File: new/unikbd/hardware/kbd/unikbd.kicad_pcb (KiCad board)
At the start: 2 copper layers, 304.8 x 152.4 mm, 140 parts, among them J1 Conn_01x16, SW1 Ampersand, SW10 Semicolon, SW11 M, SW12 J, SW14 Fwd_Slash, SW15 N, SW16 H, SW18 SPACE, SW19 B, SW20 G, SW21 ESC, SW22 Z, SW23 V, SW24 F, SW25 CTRL, SW26 A, SW27 C, SW28 D, SW29 Backslash, SW3 Break, SW30 Q, SW31 X, SW32 S, SW33 Clear, SW34 Repeat, SW35 Tilde, SW37 I, SW38 Here_is, SW39 Bracket_Close, SW4 Rubout, SW40 7, SW41 U, SW42 Shift_Lock, SW43 Bracket_Open, SW44 6, SW45 Y, SW46 Return, SW47 Dash, SW48 5, SW49 T, SW5 R_Shift, SW50 Line Feed, SW51 Colon, SW52 4, SW53 R, SW54 O, SW55 0, SW56 3, SW57 E, SW58 L, SW59 9, SW6 P, SW60 2, SW61 W, SW62 Period, SW63 8, SW64 1, SW7 Comma, SW8 K, SW9 L_Shift, U1 7402, U2 74LS240, U3 74LS240, U4 74LS373

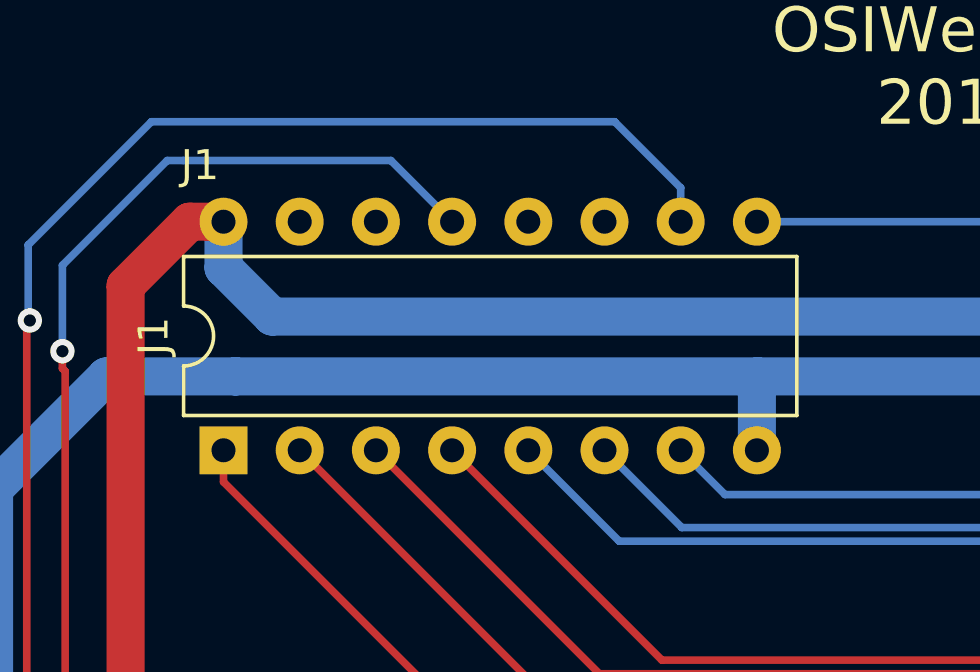
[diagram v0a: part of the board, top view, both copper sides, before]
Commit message: updated connector J1 footprint to socket
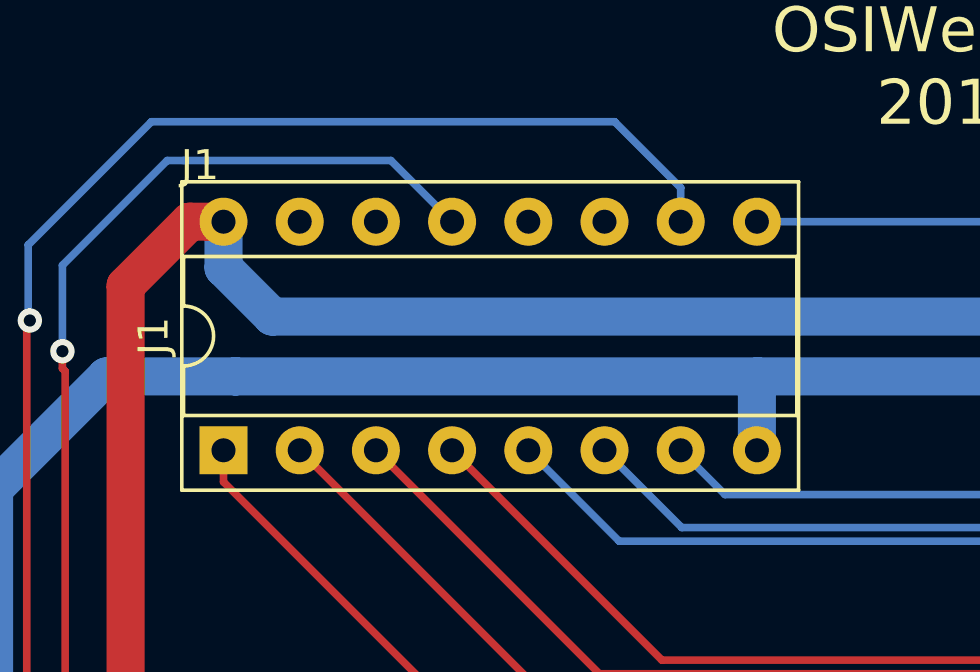
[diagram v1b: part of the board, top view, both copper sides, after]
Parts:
- J1: footprint Package_DIP:DIP-16_W7.62mm -> Package_DIP:DIP-16_W7.62mm_Socket
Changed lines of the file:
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@@
     (add_net /Col0)
+  )
+  (module Package_DIP:DIP-16_W7.62mm_Socket (layer F.Cu)
+    (at 77.9907 44.9072 90)
+    (descr "16-lead though-hole mounted DIP package, row spacing 7.62 mm (300 mils), Socket")
+    (tags "THT DIP DIL PDIP 2.54mm 7.62mm 300mil Socket")
+    (fp_text reference J1 (at 3.81 -2.33 90) (layer F.SilkS)
+      (effects (font (size 1 1) (thickness 0.15)))
+    )
+    (fp_text value Conn_01x16 (at 3.81 20.11 90) (layer F.Fab)
+      (effects (font (size 1 1) (thickness 0.15)))
+    )
+    (fp_text user %R (at 9.50214 -0.78486 180) (layer F.SilkS)
+      (effects (font (size 1 1) (thickness 0.15)))
+    )
+    (fp_line (start 9.15 -1.6) (end -1.55 -1.6) (layer F.CrtYd) (width 0.05))
+    (fp_line (start 9.15 19.4) (end 9.15 -1.6) (layer F.CrtYd) (width 0.05))
+    (fp_line (start -1.55 19.4) (end 9.15 19.4) (layer F.CrtYd) (width 0.05))
+    (fp_line (start -1.55 -1.6) (end -1.55 19.4) (layer F.CrtYd) (width 0.05))
+    (fp_line (start 8.95 -1.39) (end -1.33 -1.39) (layer F.SilkS) (width 0.12))
+    (fp_line (start 8.95 19.17) (end 8.95 -1.39) (layer F.SilkS) (width 0.12))
+    (fp_line (start -1.33 19.17) (end 8.95 19.17) (layer F.SilkS) (width 0.12))
+    (fp_line (start -1.33 -1.39) (end -1.33 19.17) (layer F.SilkS) (width 0.12))
+    (fp_line (start 6.46 -1.33) (end 4.81 -1.33) (layer F.SilkS) (width 0.12))
+    (fp_line (start 6.46 19.11) (end 6.46 -1.33) (layer F.SilkS) (width 0.12))
+    (fp_line (start 1.16 19.11) (end 6.46 19.11) (layer F.SilkS) (width 0.12))
+    (fp_line (start 1.16 -1.33) (end 1.16 19.11) (layer F.SilkS) (width 0.12))
+    (fp_line (start 2.81 -1.33) (end 1.16 -1.33) (layer F.SilkS) (width 0.12))
+    (fp_line (start 8.89 -1.33) (end -1.27 -1.33) (layer F.Fab) (width 0.1))
+    (fp_line (start 8.89 19.11) (end 8.89 -1.33) (layer F.Fab) (width 0.1))
+    (fp_line (start -1.27 19.11) (end 8.89 19.11) (layer F.Fab) (width 0.1))
+    (fp_line (start -1.27 -1.33) (end -1.27 19.11) (layer F.Fab) (width 0.1))
+    (fp_line (start 0.635 -0.27) (end 1.635 -1.27) (layer F.Fab) (width 0.1))
+    (fp_line (start 0.635 19.05) (end 0.635 -0.27) (layer F.Fab) (width 0.1))
+    (fp_line (start 6.985 19.05) (end 0.635 19.05) (layer F.Fab) (width 0.1))
+    (fp_line (start 6.985 -1.27) (end 6.985 19.05) (layer F.Fab) (width 0.1))
+    (fp_line (start 1.635 -1.27) (end 6.985 -1.27) (layer F.Fab) (width 0.1))
+    (fp_arc (start 3.81 -1.33) (end 2.81 -1.33) (angle -180) (layer F.SilkS) (width 0.12))
+    (pad 16 thru_hole oval (at 7.62 0 90) (size 1.6 1.6) (drill 0.8) (layers *.Cu *.Mask)
+      (net 2 +5V))
+    (pad 8 thru_hole oval (at 0 17.78 90) (size 1.6 1.6) (drill 0.8) (layers *.Cu *.Mask)
+      (net 1 GND))
+    (pad 15 thru_hole oval (at 7.62 2.54 90) (size 1.6 1.6) (drill 0.8) (layers *.Cu *.Mask)
+      (net 82 "Net-(J1-Pad15)"))
+    (pad 7 thru_hole oval (at 0 15.24 90) (size 1.6 1.6) (drill 0.8) (layers *.Cu *.Mask)
+      (net 81 /D6))
+    (pad 14 thru_hole oval (at 7.62 5.08 90) (size 1.6 1.6) (drill 0.8) (layers *.Cu *.Mask)
+      (net 80 "Net-(J1-Pad14)"))
+    (pad 6 thru_hole oval (at 0 12.7 90) (size 1.6 1.6) (drill 0.8) (layers *.Cu *.Mask)
+      (net 79 /D5))
+    (pad 13 thru_hole oval (at 7.62 7.62 90) (size 1.6 1.6) (drill 0.8) (layers *.Cu *.Mask)
+      (net 78 /~KBE))
+    (pad 5 thru_hole oval (at 0 10.16 90) (size 1.6 1.6) (drill 0.8) (layers *.Cu *.Mask)
+      (net 77 /D4))
+    (pad 12 thru_hole oval (at 7.62 10.16 90) (size 1.6 1.6) (drill 0.8) (layers *.Cu *.Mask)
+      (net 76 ~A1))
+    (pad 4 thru_hole oval (at 0 7.62 90) (size 1.6 1.6) (drill 0.8) (layers *.Cu *.Mask)
+      (net 75 /D3))
+    (pad 11 thru_hole oval (at 7.62 12.7 90) (size 1.6 1.6) (drill 0.8) (layers *.Cu *.Mask)
+      (net 74 ~A0))
+    (pad 3 thru_hole oval (at 0 5.08 90) (size 1.6 1.6) (drill 0.8) (layers *.Cu *.Mask)
+      (net 73 /D2))
+    (pad 10 thru_hole oval (at 7.62 15.24 90) (size 1.6 1.6) (drill 0.8) (layers *.Cu *.Mask)
+      (net 72 /R_~W))
+    (pad 2 thru_hole oval (at 0 2.54 90) (size 1.6 1.6) (drill 0.8) (layers *.Cu *.Mask)
+      (net 71 /D1))
+    (pad 9 thru_hole oval (at 7.62 17.78 90) (size 1.6 1.6) (drill 0.8) (layers *.Cu *.Mask)
+      (net 70 /D7))
+    (pad 1 thru_hole rect (at 0 0 90) (size 1.6 1.6) (drill 0.8) (layers *.Cu *.Mask)
+      (net 114 /D0))
+    (model ${KISYS3DMOD}/Package_DIP.3dshapes/DIP-16_W7.62mm_Socket.wrl
+      (at (xyz 0 0 0))
+      (scale (xyz 1 1 1))
+      (rotate (xyz 0 0 0))
+    )
   )
   (module Resistor_THT:R_Array_SIP9 (layer F.Cu)
@@
       (at (xyz 0 0 0))
       (scale (xyz 1 1 1))
-      (rotate (xyz 0 0 0))
-    )
-  )
-  (module Package_DIP:DIP-16_W7.62mm (layer F.Cu)
-    (at 77.9907 44.9072 90)
-    (descr "16-lead though-hole mounted DIP package, row spacing 7.62 mm (300 mils)")
-    (tags "THT DIP DIL PDIP 2.54mm 7.62mm 300mil")
-    (fp_text reference J1 (at 3.81 -2.33 90) (layer F.SilkS)
-      (effects (font (size 1 1) (thickness 0.15)))
-    )
-    (fp_text value Conn_01x16 (at 3.81 20.11 90) (layer F.Fab)
-      (effects (font (size 1 1) (thickness 0.15)))
-    )
-    (fp_arc (start 3.81 -1.33) (end 2.81 -1.33) (angle -180) (layer F.SilkS) (width 0.12))
-    (fp_line (start 1.635 -1.27) (end 6.985 -1.27) (layer F.Fab) (width 0.1))
-    (fp_line (start 6.985 -1.27) (end 6.985 19.05) (layer F.Fab) (width 0.1))
-    (fp_line (start 6.985 19.05) (end 0.635 19.05) (layer F.Fab) (width 0.1))
-    (fp_line (start 0.635 19.05) (end 0.635 -0.27) (layer F.Fab) (width 0.1))
-    (fp_line (start 0.635 -0.27) (end 1.635 -1.27) (layer F.Fab) (width 0.1))
-    (fp_line (start 2.81 -1.33) (end 1.16 -1.33) (layer F.SilkS) (width 0.12))
-    (fp_line (start 1.16 -1.33) (end 1.16 19.11) (layer F.SilkS) (width 0.12))
-    (fp_line (start 1.16 19.11) (end 6.46 19.11) (layer F.SilkS) (width 0.12))
-    (fp_line (start 6.46 19.11) (end 6.46 -1.33) (layer F.SilkS) (width 0.12))
-    (fp_line (start 6.46 -1.33) (end 4.81 -1.33) (layer F.SilkS) (width 0.12))
-    (fp_line (start -1.1 -1.55) (end -1.1 19.3) (layer F.CrtYd) (width 0.05))
-    (fp_line (start -1.1 19.3) (end 8.7 19.3) (layer F.CrtYd) (width 0.05))
-    (fp_line (start 8.7 19.3) (end 8.7 -1.55) (layer F.CrtYd) (width 0.05))
-    (fp_line (start 8.7 -1.55) (end -1.1 -1.55) (layer F.CrtYd) (width 0.05))
-    (fp_text user %R (at 9.50214 -0.78486 180) (layer F.SilkS)
-      (effects (font (size 1 1) (thickness 0.15)))
-    )
-    (pad 1 thru_hole rect (at 0 0 90) (size 1.6 1.6) (drill 0.8) (layers *.Cu *.Mask)
-      (net 114 /D0))
-    (pad 9 thru_hole oval (at 7.62 17.78 90) (size 1.6 1.6) (drill 0.8) (layers *.Cu *.Mask)
-      (net 70 /D7))
-    (pad 2 thru_hole oval (at 0 2.54 90) (size 1.6 1.6) (drill 0.8) (layers *.Cu *.Mask)
-      (net 71 /D1))
-    (pad 10 thru_hole oval (at 7.62 15.24 90) (size 1.6 1.6) (drill 0.8) (layers *.Cu *.Mask)
-      (net 72 /R_~W))
-    (pad 3 thru_hole oval (at 0 5.08 90) (size 1.6 1.6) (drill 0.8) (layers *.Cu *.Mask)
-      (net 73 /D2))
-    (pad 11 thru_hole oval (at 7.62 12.7 90) (size 1.6 1.6) (drill 0.8) (layers *.Cu *.Mask)
-      (net 74 ~A0))
-    (pad 4 thru_hole oval (at 0 7.62 90) (size 1.6 1.6) (drill 0.8) (layers *.Cu *.Mask)
-      (net 75 /D3))
-    (pad 12 thru_hole oval (at 7.62 10.16 90) (size 1.6 1.6) (drill 0.8) (layers *.Cu *.Mask)
-      (net 76 ~A1))
-    (pad 5 thru_hole oval (at 0 10.16 90) (size 1.6 1.6) (drill 0.8) (layers *.Cu *.Mask)
-      (net 77 /D4))
-    (pad 13 thru_hole oval (at 7.62 7.62 90) (size 1.6 1.6) (drill 0.8) (layers *.Cu *.Mask)
-      (net 78 /~KBE))
-    (pad 6 thru_hole oval (at 0 12.7 90) (size 1.6 1.6) (drill 0.8) (layers *.Cu *.Mask)
-      (net 79 /D5))
-    (pad 14 thru_hole oval (at 7.62 5.08 90) (size 1.6 1.6) (drill 0.8) (layers *.Cu *.Mask)
-      (net 80 "Net-(J1-Pad14)"))
-    (pad 7 thru_hole oval (at 0 15.24 90) (size 1.6 1.6) (drill 0.8) (layers *.Cu *.Mask)
-      (net 81 /D6))
-    (pad 15 thru_hole oval (at 7.62 2.54 90) (size 1.6 1.6) (drill 0.8) (layers *.Cu *.Mask)
-      (net 82 "Net-(J1-Pad15)"))
-    (pad 8 thru_hole oval (at 0 17.78 90) (size 1.6 1.6) (drill 0.8) (layers *.Cu *.Mask)
-      (net 1 GND))
-    (pad 16 thru_hole oval (at 7.62 0 90) (size 1.6 1.6) (drill 0.8) (layers *.Cu *.Mask)
-      (net 2 +5V))
-    (model ${KISYS3DMOD}/Package_DIP.3dshapes/DIP-16_W7.62mm.wrl
-      (at (xyz 0 0 0))
-      (scale (xyz 1 1 1))

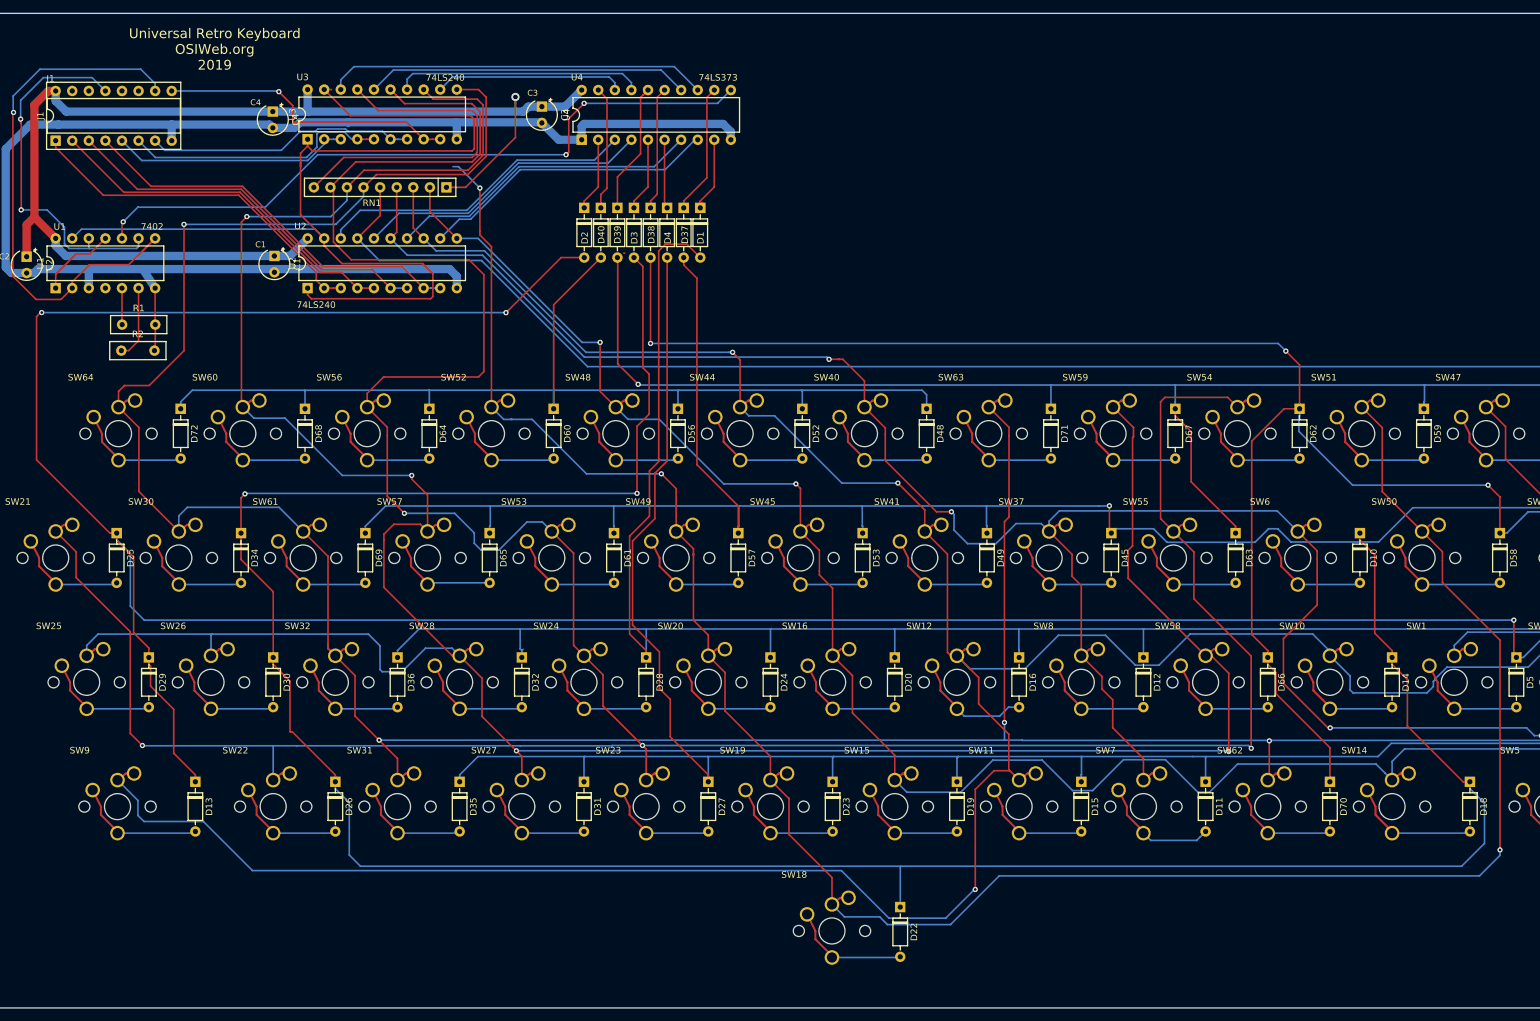
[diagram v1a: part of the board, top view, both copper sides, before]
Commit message: OSI 542 clone with 16-pin header extension
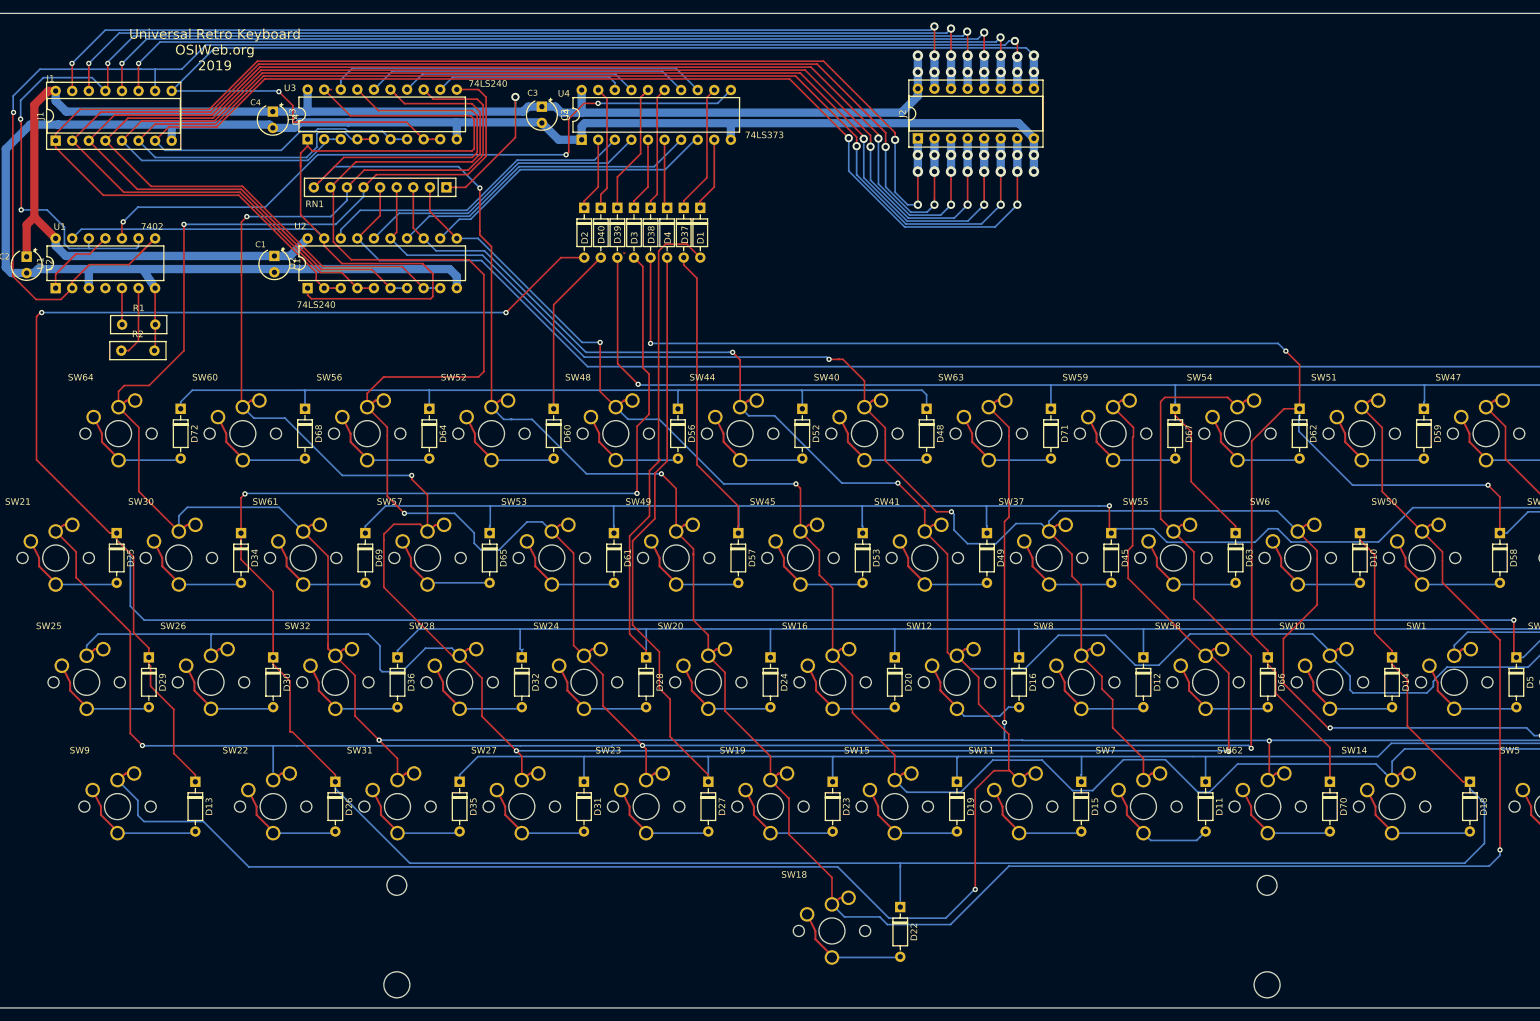
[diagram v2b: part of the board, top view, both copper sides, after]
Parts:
- added J2: Conn_01x16, Package_DIP:DIP-16_W7.62mm_Socket, F.Cu at (210.1, 44.6)
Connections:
- J1 pad 11: ~A0 -> /~A0
- J1 pad 12: ~A1 -> /~A1
- J1 pad 14: Net-(J1-Pad14) -> /NI
- J1 pad 15: Net-(J1-Pad15) -> /~SI
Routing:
- net /D0: track 54.3 -> 216.7 mm, vias 0 -> 4
- net /D1: track 55.6 -> 217.9 mm, vias 0 -> 4
- net /D2: track 58.1 -> 219.6 mm, vias 0 -> 4
- net /D3: track 60.7 -> 221.7 mm, vias 0 -> 4
- net /D4: track 36.6 -> 197.2 mm, vias 0 -> 4
- net /D5: track 40.4 -> 200.8 mm, vias 0 -> 4
- net /D6: track 41.2 -> 201.2 mm, vias 0 -> 4
- net /~SI: track 0.00 -> 148.3 mm, vias 0 -> 4
- net /NI: track 0.00 -> 147.8 mm, vias 0 -> 4
- net /~KBE: track 57.0 -> 203.9 mm, vias 2 -> 6
- net /~A1: track 0.00 -> 146.9 mm, vias 0 -> 4
- net /~A0: track 0.00 -> 145.8 mm, vias 0 -> 4
- net /R_~W: track 84.6 -> 227.2 mm, vias 1 -> 4
- net /D7: track 45.7 -> 186.1 mm, vias 1 -> 3
- net +5V: track 183.5 -> 245.1 mm, vias 1 -> 3
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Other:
- outline, holes or cut-outs redrawn
